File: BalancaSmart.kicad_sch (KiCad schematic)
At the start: 56 parts, among them J1 Load Cell, J2 Barrel_Jack, Q1 PMOS, Q2 NMOS, Q3 NMOS, Q4 S8050, SW1 SW_Push, SW2 SW_SPDT, U1 HX711-Mod, U2 ADS1115-module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

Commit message: adicionado footprint do ADS1115, continuação do desenvolvimento do layout da pcb
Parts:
- J1: footprint Connector_PinHeader_2.54mm:PinHeader_1x04_P2.54mm_Vertical -> TerminalBlock:TerminalBlock_MaiXu_MX126-5.0-04P_1x04_P5.00mm
- U2: footprint (none) -> project_library:ADS1115 Module
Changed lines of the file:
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@@
 			)
 		)
-		(property "Footprint" "Connector_PinHeader_2.54mm:PinHeader_1x04_P2.54mm_Vertical"
+		(property "Footprint" "TerminalBlock:TerminalBlock_MaiXu_MX126-5.0-04P_1x04_P5.00mm"
 			(at 17.78 36.83 0)
 			(hide yes)
@@
 			)
 		)
-		(property "Footprint" ""
+		(property "Footprint" "project_library:ADS1115 Module"
 			(at 177.8 124.46 0)
 			(hide yes)

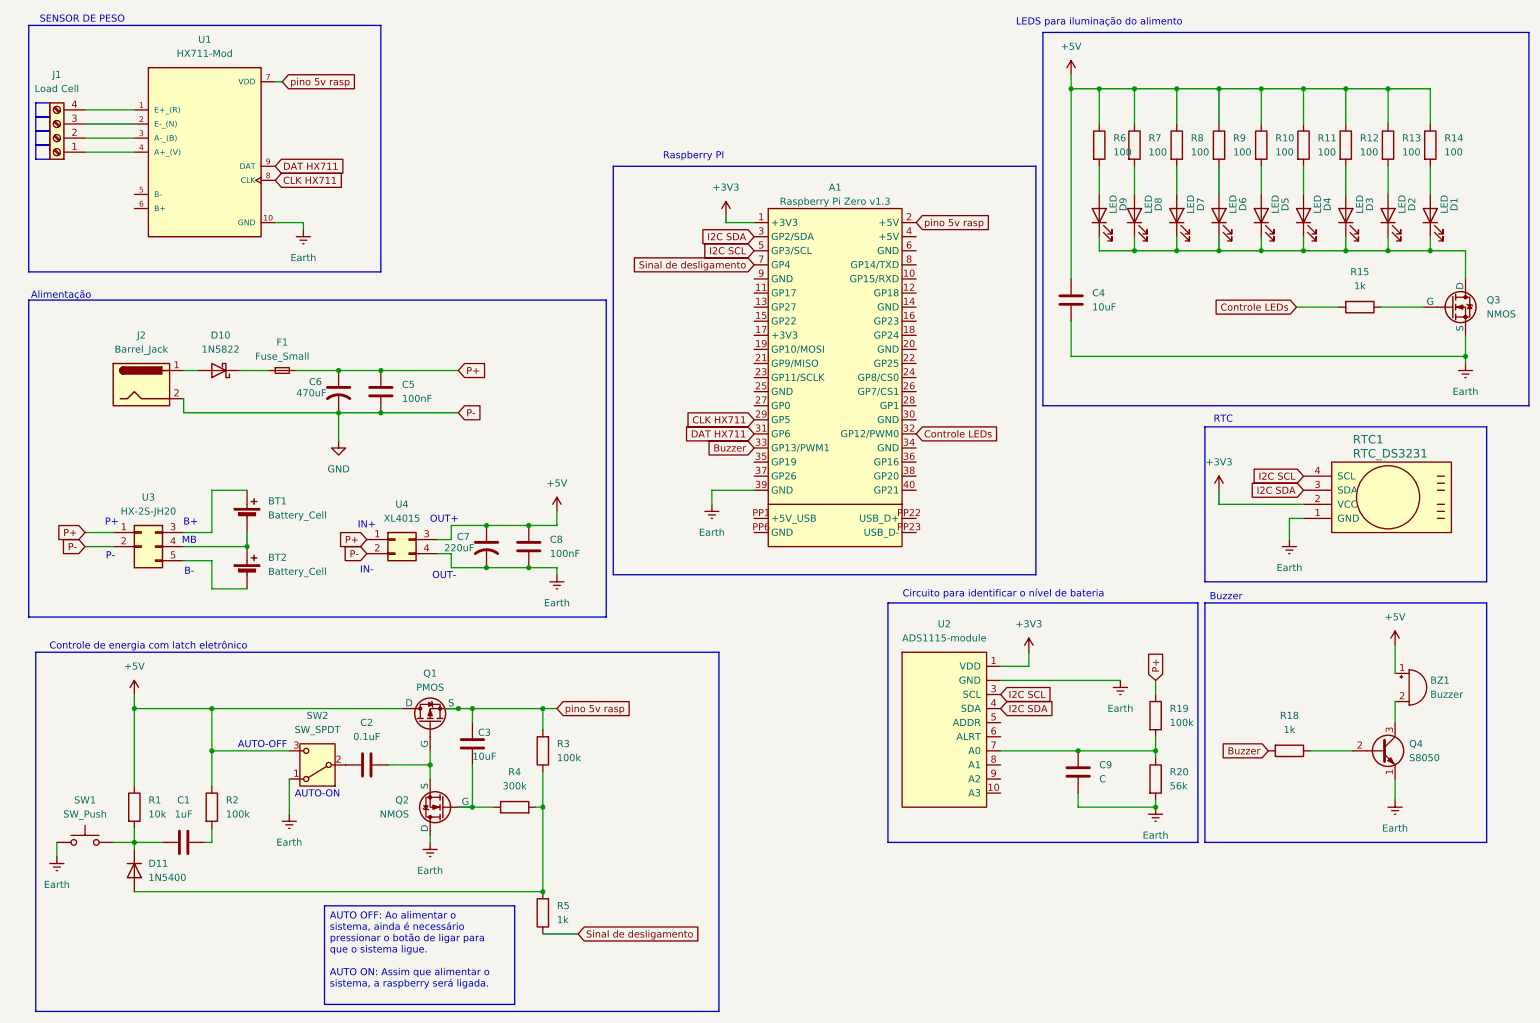
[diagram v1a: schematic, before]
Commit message: designação de footprints
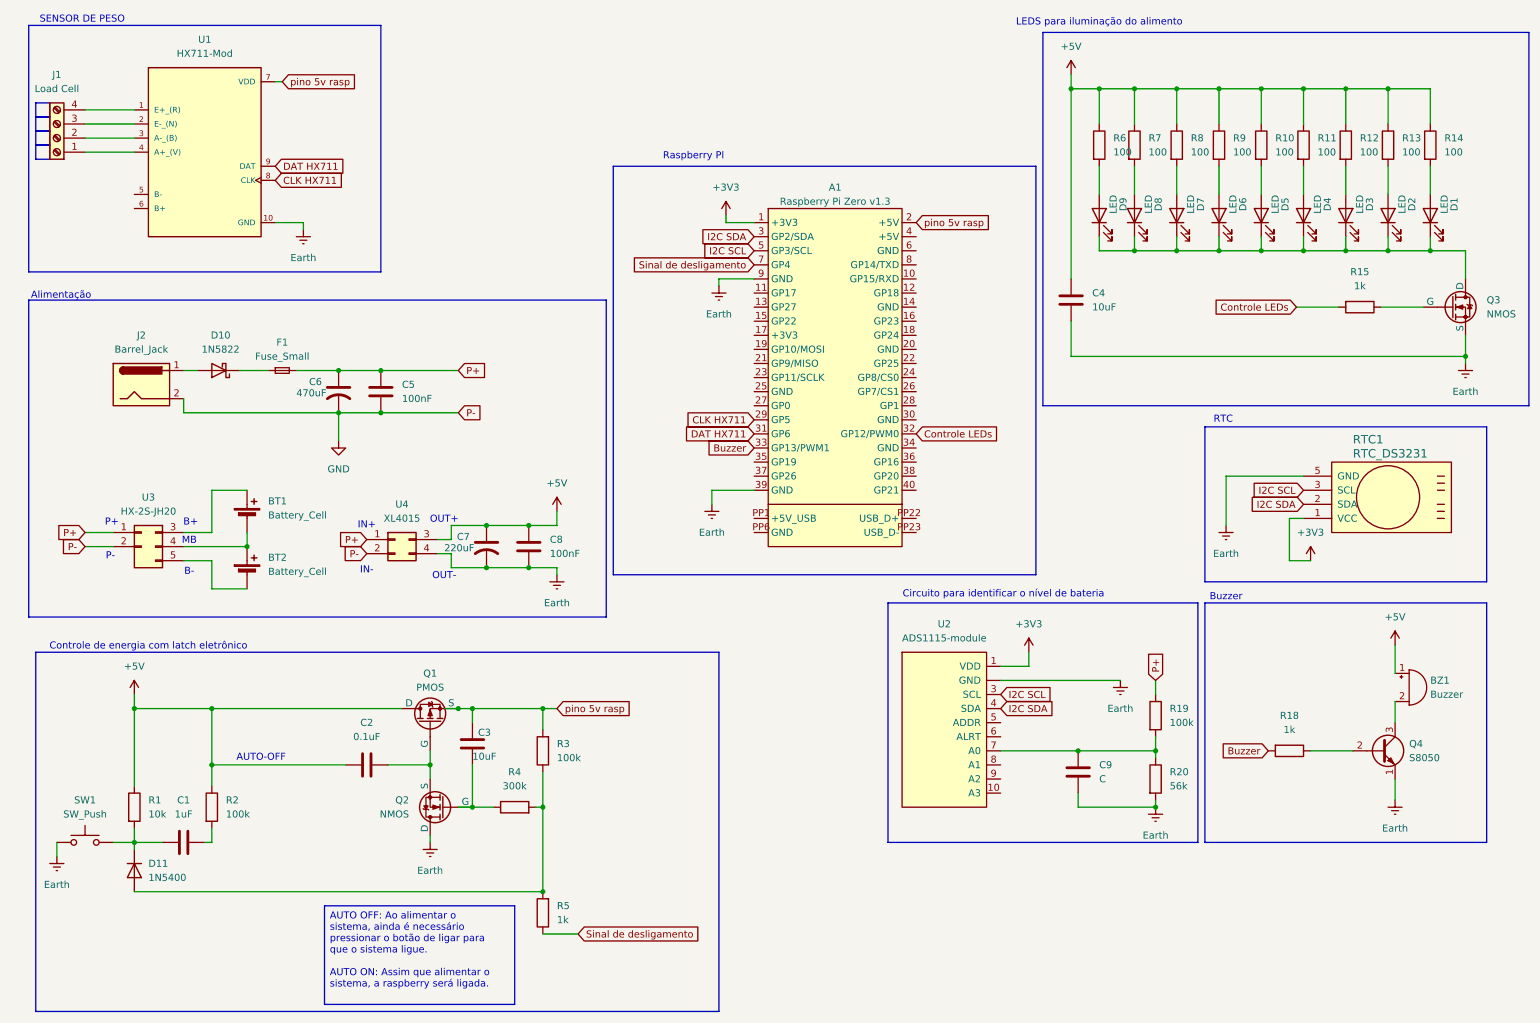
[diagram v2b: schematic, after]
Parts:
- removed SW2: SW_SPDT, symbol Switch:SW_SPDT
- D1, D2, D3, D4, D5, D6, D7, D8, D9: footprint (none) -> Connector_PinHeader_2.54mm:PinHeader_1x02_P2.54mm_Vertical
- J2: footprint (none) -> TerminalBlock:TerminalBlock_MaiXu_MX126-5.0-02P_1x02_P5.00mm
- Q1, Q2, Q3: footprint (none) -> Package_TO_SOT_THT:TO-220-3_Vertical
- R1, R10, R11, R12, R13, R14, R15, R18, R19, R2, R20, R3, R4, R5, R6, R7, R8, R9: footprint (none) -> Resistor_THT:R_Axial_DIN0204_L3.6mm_D1.6mm_P7.62mm_Horizontal
- RTC1: footprint (none) -> Connector_PinHeader_2.54mm:PinHeader_1x05_P2.54mm_Vertical
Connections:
- net +3V3: now also RTC1.1 (VCC); no longer RTC1.2 (VCC)
- net +5V: now also C2.1
- net Earth: now also A1.9 (GND), RTC1.5 (GND); no longer RTC1.1 (GND)
- net I2C SCL: now also RTC1.3 (SCL); no longer RTC1.4 (SCL)
- net I2C SDA: now also RTC1.2 (SDA); no longer RTC1.3 (SDA)
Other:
- note removed: "AUTO-ON"

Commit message: layout do circuito dos leds
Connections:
- net +5V: now also R10.2, R11.2, R12.2, R13.2, R14.2, R6.2, R7.2, R8.2, R9.2; no longer R10.1, R11.1, R12.1, R13.1, R14.1, R6.1, R7.1, R8.1, R9.1
- net at D5.2 (A): now also R10.1; no longer R10.2
- net at D4.2 (A): now also R11.1; no longer R11.2
- net at D3.2 (A): now also R12.1; no longer R12.2
- net at D2.2 (A): now also R13.1; no longer R13.2
- net at D1.2 (A): now also R14.1; no longer R14.2
- net at D7.2 (A): now also R8.1; no longer R8.2
- net at D6.2 (A): now also R9.1; no longer R9.2
- net at D8.2 (A): now also R7.1; no longer R7.2
- net at D9.2 (A): now also R6.1; no longer R6.2
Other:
- moved on the sheet: R10, R11, R12, R13, R14, R6, R7, R8, R9
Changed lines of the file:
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@@
 	)
 	(junction
-		(at 90.17 139.7)
-		(diameter 0)
-		(color 0 0 0 0)
-	)
-	(junction
 		(at 257.81 57.15)
 		(diameter 0)
@@
 	)
 	(junction
-		(at 92.71 139.7)
-		(diameter 0)
-		(color 0 0 0 0)
-	)
-	(junction
 		(at 234.95 57.15)
 		(diameter 0)
@@
 	)
 	(junction
+		(at 92.71 139.7)
+		(diameter 0)
+		(color 0 0 0 0)
+	)
+	(junction
 		(at 201.93 147.32)
 		(diameter 0)
@@
 	(wire
 		(pts
-			(xy 87.63 139.7) (xy 90.17 139.7)
-		)
-		(stroke
-			(width 0)
-			(type default)
-		)
-	)
-	(wire
-		(pts
 			(xy 107.95 114.3) (xy 102.87 114.3)
 		)
@@
 	(wire
 		(pts
-			(xy 90.17 139.7) (xy 92.71 139.7)
-		)
-		(stroke
-			(width 0)
-			(type default)
-		)
-	)
-	(wire
-		(pts
 			(xy 45.72 118.11) (xy 52.07 118.11)
 		)
@@
 	(wire
 		(pts
+			(xy 90.17 139.7) (xy 92.71 139.7)
+		)
+		(stroke
+			(width 0)
+			(type default)
+		)
+	)
+	(wire
+		(pts
 			(xy 31.75 163.83) (xy 36.83 163.83)
 		)
@@
 	(symbol
 		(lib_id "Device:R")
-		(at 242.57 38.1 0)
+		(at 242.57 38.1 180)
 		(unit 1)
 		(body_style 1)
@@
 					(size 1.27 1.27)
 				)
-				(justify left)
+				(justify right)
 			)
 		)
@@
 					(size 1.27 1.27)
 				)
-				(justify left)
+				(justify right)
 			)
 		)
 		(property "Footprint" "Resistor_THT:R_Axial_DIN0204_L3.6mm_D1.6mm_P7.62mm_Horizontal"
-			(at 240.792 38.1 90)
+			(at 244.348 38.1 90)
 			(hide yes)
 			(show_name no)
@@
 	(symbol
 		(lib_id "Device:R")
-		(at 250.19 38.1 0)
+		(at 250.19 38.1 180)
 		(unit 1)
 		(body_style 1)
@@
 					(size 1.27 1.27)
 				)
-				(justify left)
+				(justify right)
 			)
 		)
@@
 					(size 1.27 1.27)
 				)
-				(justify left)
+				(justify right)
 			)
 		)
 		(property "Footprint" "Resistor_THT:R_Axial_DIN0204_L3.6mm_D1.6mm_P7.62mm_Horizontal"
-			(at 248.412 38.1 90)
+			(at 251.968 38.1 90)
 			(hide yes)
 			(show_name no)
@@
 	(symbol
 		(lib_id "Device:R")
-		(at 234.95 38.1 0)
+		(at 234.95 38.1 180)
 		(unit 1)
 		(body_style 1)
@@
 					(size 1.27 1.27)
 				)
-				(justify left)
+				(justify right)
 			)
 		)
@@
 					(size 1.27 1.27)
 				)
-				(justify left)
+				(justify right)
 			)
 		)
 		(property "Footprint" "Resistor_THT:R_Axial_DIN0204_L3.6mm_D1.6mm_P7.62mm_Horizontal"
-			(at 233.172 38.1 90)
+			(at 236.728 38.1 90)
 			(hide yes)
 			(show_name no)
@@
 	(symbol
 		(lib_id "Device:R")
-		(at 219.71 38.1 0)
+		(at 219.71 38.1 180)
 		(unit 1)
 		(body_style 1)
@@
 					(size 1.27 1.27)
 				)
-				(justify left)
+				(justify right)
 			)
 		)
@@
 					(size 1.27 1.27)
 				)
-				(justify left)
+				(justify right)
 			)
 		)
 		(property "Footprint" "Resistor_THT:R_Axial_DIN0204_L3.6mm_D1.6mm_P7.62mm_Horizontal"
-			(at 217.932 38.1 90)
+			(at 221.488 38.1 90)
 			(hide yes)
 			(show_name no)
@@
 	(symbol
 		(lib_id "Device:R")
-		(at 212.09 38.1 0)
+		(at 212.09 38.1 180)
 		(unit 1)
 		(body_style 1)
@@
 					(size 1.27 1.27)
 				)
-				(justify left)
+				(justify right)
 			)
 		)
@@
 					(size 1.27 1.27)
 				)
-				(justify left)
+				(justify right)
 			)
 		)
 		(property "Footprint" "Resistor_THT:R_Axial_DIN0204_L3.6mm_D1.6mm_P7.62mm_Horizontal"
-			(at 210.312 38.1 90)
+			(at 213.868 38.1 90)
 			(hide yes)
 			(show_name no)
@@
 	(symbol
 		(lib_id "Device:R")
-		(at 205.74 38.1 0)
+		(at 205.74 38.1 180)
 		(unit 1)
 		(body_style 1)
@@
 					(size 1.27 1.27)
 				)
-				(justify left)
+				(justify right)
 			)
 		)
@@
 					(size 1.27 1.27)
 				)
-				(justify left)
+				(justify right)
 			)
 		)
 		(property "Footprint" "Resistor_THT:R_Axial_DIN0204_L3.6mm_D1.6mm_P7.62mm_Horizontal"
-			(at 203.962 38.1 90)
+			(at 207.518 38.1 90)
 			(hide yes)
 			(show_name no)
@@
 	(symbol
 		(lib_id "Device:R")
-		(at 265.43 38.1 0)
+		(at 265.43 38.1 180)
 		(unit 1)
 		(body_style 1)
@@
 					(size 1.27 1.27)
 				)
-				(justify left)
+				(justify right)
 			)
 		)
@@
 					(size 1.27 1.27)
 				)
-				(justify left)
+				(justify right)
 			)
 		)
 		(property "Footprint" "Resistor_THT:R_Axial_DIN0204_L3.6mm_D1.6mm_P7.62mm_Horizontal"
-			(at 263.652 38.1 90)
+			(at 267.208 38.1 90)
 			(hide yes)
 			(show_name no)
@@
 	(symbol
 		(lib_id "Device:R")
-		(at 227.33 38.1 0)
+		(at 227.33 38.1 180)
 		(unit 1)
 		(body_style 1)
@@
 					(size 1.27 1.27)
 				)
-				(justify left)
+				(justify right)
 			)
 		)
@@
 					(size 1.27 1.27)
 				)
-				(justify left)
+				(justify right)
 			)
 		)
 		(property "Footprint" "Resistor_THT:R_Axial_DIN0204_L3.6mm_D1.6mm_P7.62mm_Horizontal"
-			(at 225.552 38.1 90)
+			(at 229.108 38.1 90)
 			(hide yes)
 			(show_name no)
@@
 	(symbol
 		(lib_id "Device:R")
-		(at 257.81 38.1 0)
+		(at 257.81 38.1 180)
 		(unit 1)
 		(body_style 1)
@@
 					(size 1.27 1.27)
 				)
-				(justify left)
+				(justify right)
 			)
 		)
@@
 					(size 1.27 1.27)
 				)
-				(justify left)
+				(justify right)
 			)
 		)
 		(property "Footprint" "Resistor_THT:R_Axial_DIN0204_L3.6mm_D1.6mm_P7.62mm_Horizontal"
-			(at 256.032 38.1 90)
+			(at 259.588 38.1 90)
 			(hide yes)
 			(show_name no)

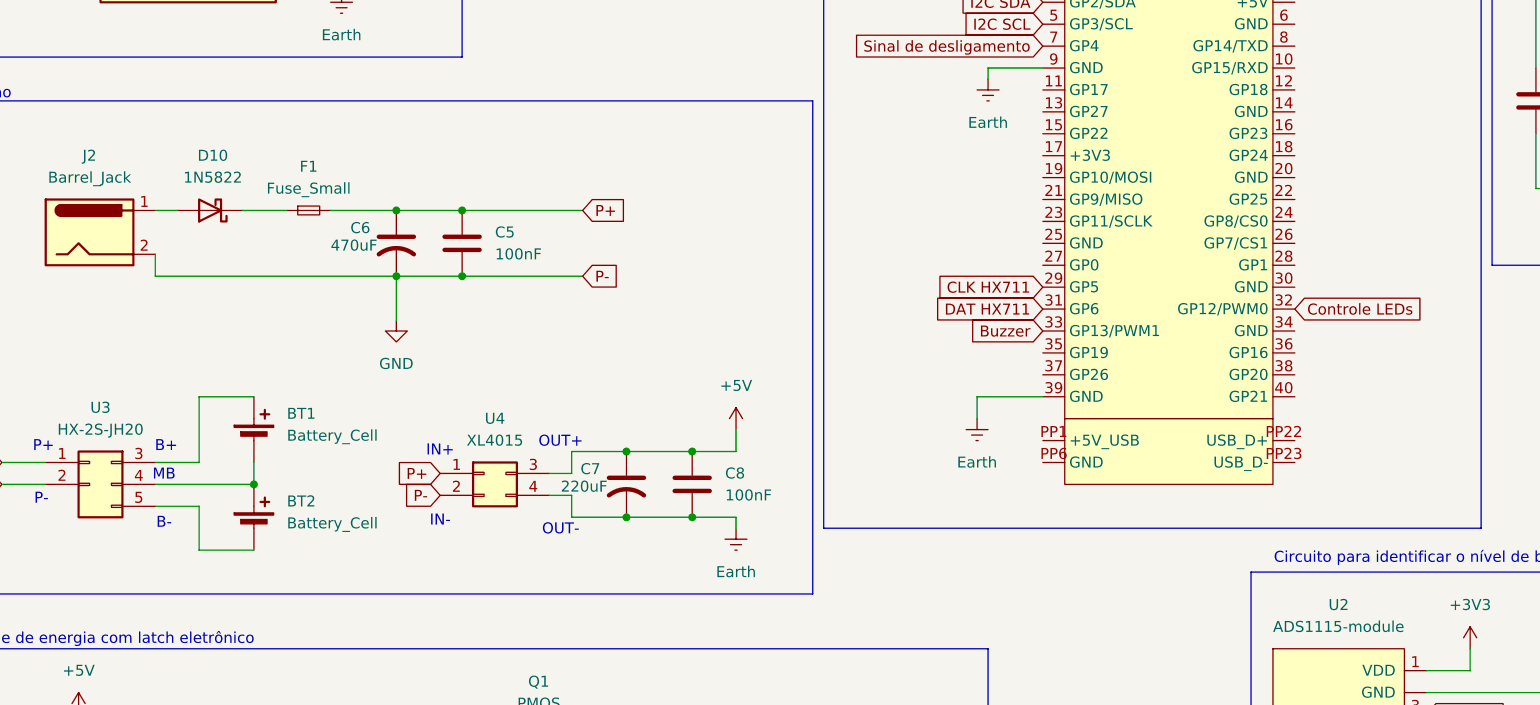
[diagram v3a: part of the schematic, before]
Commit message: continuação do layout da PCB e designação de footprints
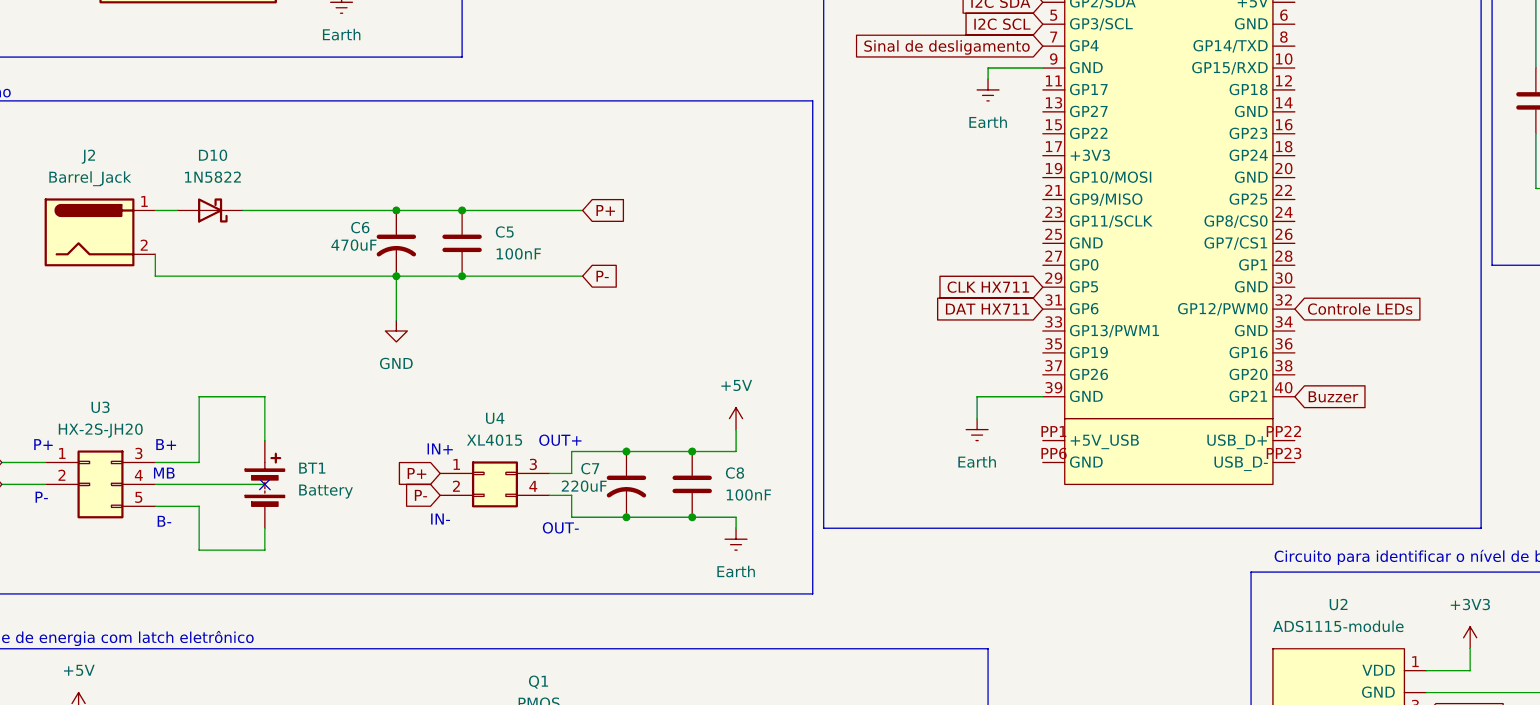
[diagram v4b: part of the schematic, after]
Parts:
- removed BT1, BT2: Battery_Cell, symbol Device:Battery_Cell
- removed F1: Fuse_Small, symbol Device:Fuse_Small
- added BT1: Battery, TerminalBlock:TerminalBlock_MaiXu_MX126-5.0-02P_1x02_P5.00mm, symbol Device:Battery
- BZ1: footprint (none) -> Buzzer_Beeper:MagneticBuzzer_PUI_AT-0927-TT-6-R
- C2, C5, C8: footprint (none) -> Capacitor_THT:C_Disc_D5.0mm_W2.5mm_P2.50mm
- C6, C7: footprint (none) -> Capacitor_THT:C_Radial_D6.3mm_H7.0mm_P2.50mm
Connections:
- net Buzzer: now also A1.40 (GP21); no longer A1.33 (GP13/PWM1)
- net P+: now also D10.1 (K)
- net at U3.3 (B+): now also BT1.1 (+)
- net at U3.5 (B-): now also BT1.2 (-)
- no-connect marks 0 -> 1

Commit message: continuação pcb
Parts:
- C1, C3, C4, C9: footprint (none) -> Capacitor_THT:C_Radial_D6.3mm_H7.0mm_P2.50mm
- U3, U4: footprint (none) -> TerminalBlock:TerminalBlock_MaiXu_MX126-5.0-04P_1x04_P5.00mm
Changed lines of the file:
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@@
 			)
 		)
-		(property "Footprint" ""
+		(property "Footprint" "TerminalBlock:TerminalBlock_MaiXu_MX126-5.0-04P_1x04_P5.00mm"
 			(at 78.74 109.22 0)
 			(hide yes)
@@
 			)
 		)
-		(property "Footprint" ""
+		(property "Footprint" "Capacitor_THT:C_Radial_D6.3mm_H7.0mm_P2.50mm"
 			(at 201.6252 69.85 0)
 			(hide yes)
@@
 			)
 		)
-		(property "Footprint" ""
+		(property "Footprint" "Capacitor_THT:C_Radial_D6.3mm_H7.0mm_P2.50mm"
 			(at 202.8952 154.94 0)
 			(hide yes)
@@
 			)
 		)
-		(property "Footprint" ""
+		(property "Footprint" "TerminalBlock:TerminalBlock_MaiXu_MX126-5.0-04P_1x04_P5.00mm"
 			(at 35.56 110.49 0)
 			(hide yes)
@@
 			)
 		)
-		(property "Footprint" ""
+		(property "Footprint" "Capacitor_THT:C_Radial_D6.3mm_H7.0mm_P2.50mm"
 			(at 91.7448 142.24 0)
 			(hide yes)
@@
 			)
 		)
-		(property "Footprint" ""
+		(property "Footprint" "Capacitor_THT:C_Radial_D6.3mm_H7.0mm_P2.50mm"
 			(at 44.45 162.8648 0)
 			(hide yes)

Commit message: layout PCB finalizado
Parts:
- added JP1: Jumper_2_Bridged, Resistor_THT:R_Axial_DIN0204_L3.6mm_D1.6mm_P7.62mm_Horizontal, symbol Jumper:Jumper_2_Bridged
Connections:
- net Earth: now also A1.6 (GND), JP1.2 (B); no longer A1.39 (GND), A1.9 (GND), C7.2, C8.2, Q2.1 (D), SW1.1, U4.4 (Pin_4)
- net GND: now also C7.2, C8.2, Q2.1 (D), SW1.1, U4.4 (Pin_4), JP1.1 (A)
